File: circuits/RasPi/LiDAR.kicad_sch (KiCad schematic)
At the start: 2 parts, among them J6 Conn_01x03_MountingPin, J9 Conn_01x04_MountingPin

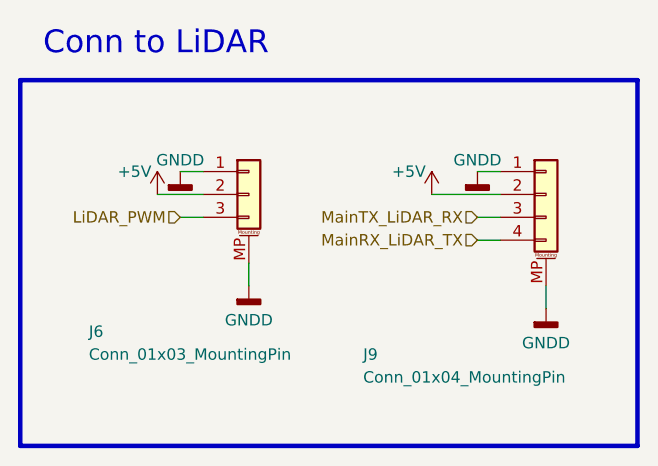
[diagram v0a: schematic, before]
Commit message: 発注第2弾
RasPi発注
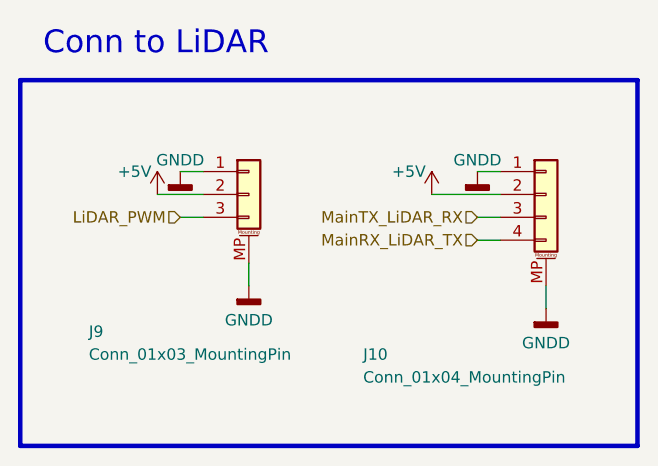
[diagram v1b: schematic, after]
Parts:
- renumbered J9 to J10, J6 to J9
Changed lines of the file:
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@@
   (symbol (lib_id "Connector_Generic_MountingPin:Conn_01x03_MountingPin") (at 129.54 76.2 0) (unit 1)
     (in_bom yes) (on_board yes) (dnp no)
-    (property "Reference" "J6" (at 111.76 91.44 0)
+    (property "Reference" "J9" (at 111.76 91.44 0)
       (effects (font (size 1.27 1.27)) (justify left))
     )
@@
       (project "RasPi"
         (path "/689a9e74-f202-4ea4-bfbb-4341f2549250/fddad0c3-2af8-46e3-8794-fa1122d24d51/ac6ce566-f0cf-4831-8e6b-6ce1bd313790"
-          (reference "J6") (unit 1)
+          (reference "J9") (unit 1)
         )
       )
@@
   (symbol (lib_id "Connector_Generic_MountingPin:Conn_01x04_MountingPin") (at 162.56 76.2 0) (unit 1)
     (in_bom yes) (on_board yes) (dnp no)
-    (property "Reference" "J9" (at 142.24 93.98 0)
+    (property "Reference" "J10" (at 142.24 93.98 0)
       (effects (font (size 1.27 1.27)) (justify left))
     )
@@
       (project "RasPi"
         (path "/689a9e74-f202-4ea4-bfbb-4341f2549250/fddad0c3-2af8-46e3-8794-fa1122d24d51/ac6ce566-f0cf-4831-8e6b-6ce1bd313790"
-          (reference "J9") (unit 1)
+          (reference "J10") (unit 1)
         )
       )
